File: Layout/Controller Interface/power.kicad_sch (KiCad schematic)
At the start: 26 parts, among them J6 Conn_01x02_Pin, Q1 AO3401A, Q2 AO3401A, Q3 AO3401A, Q4 AO3400A, Q5 AO3400A, SW5 SW_Push_Dual, U2 LM3671MF, U4 MCP73812T-420I-OT, U5 TPS613222ADBZ

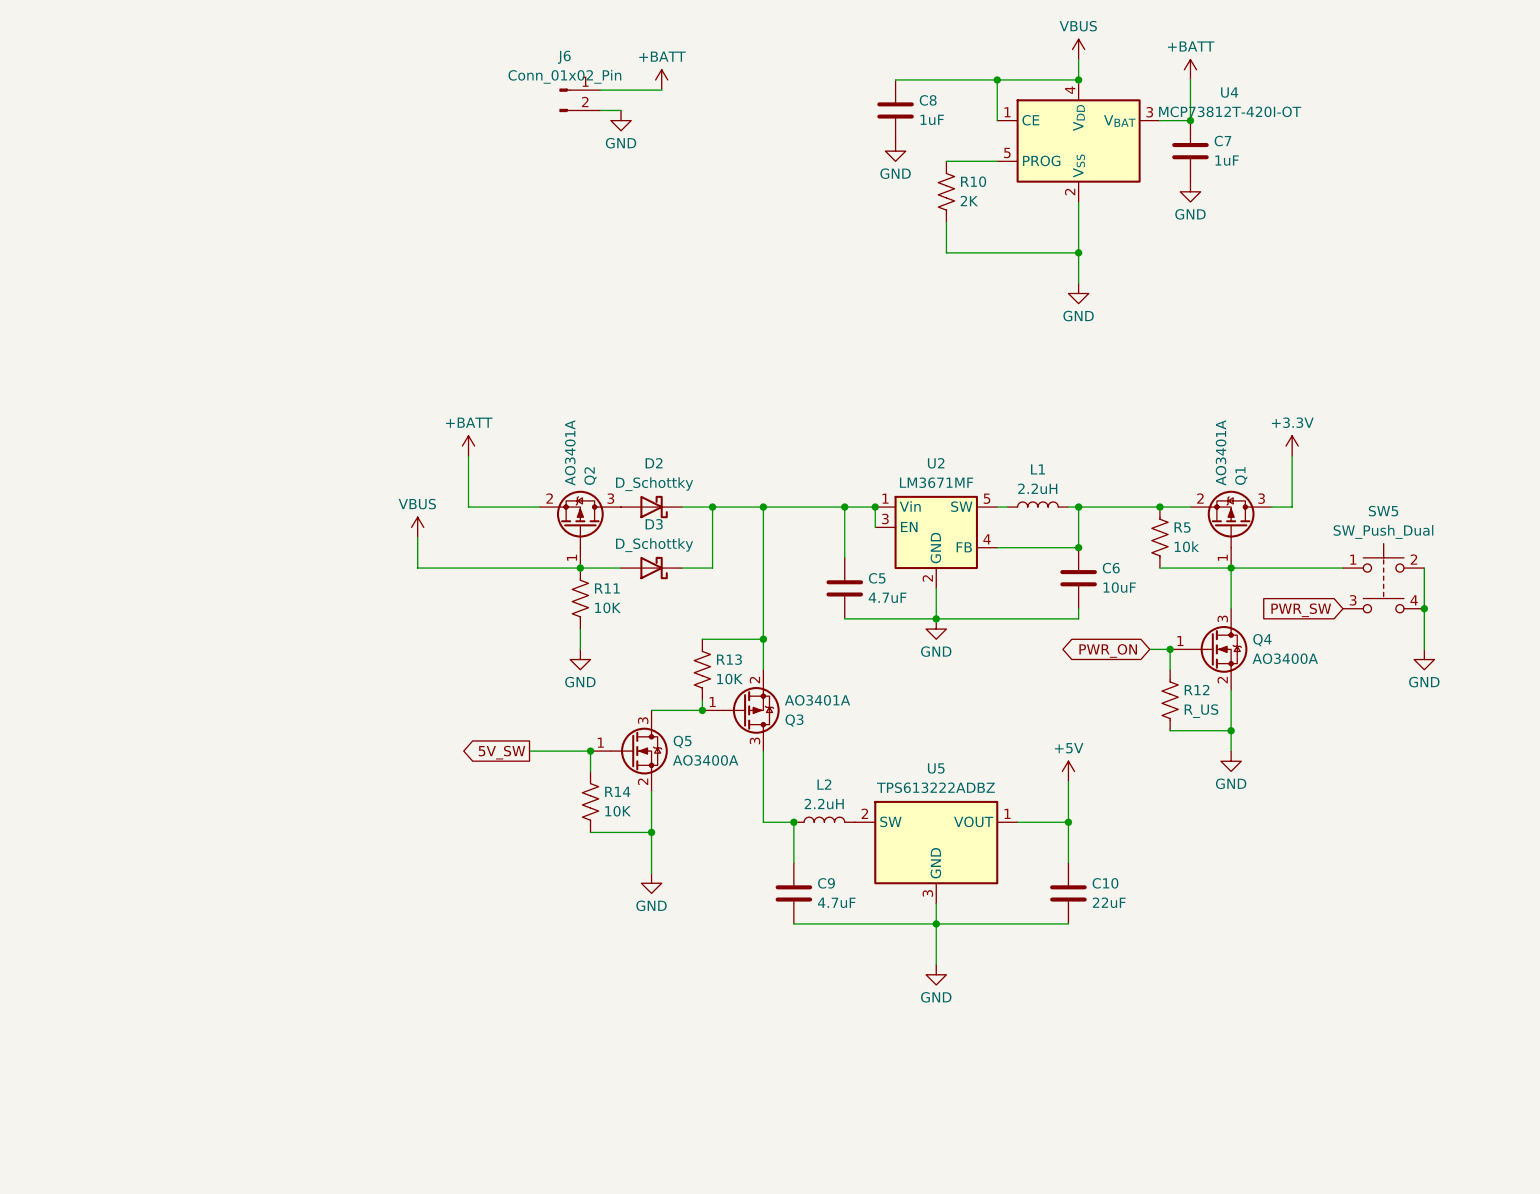
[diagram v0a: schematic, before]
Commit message: Schematic updates
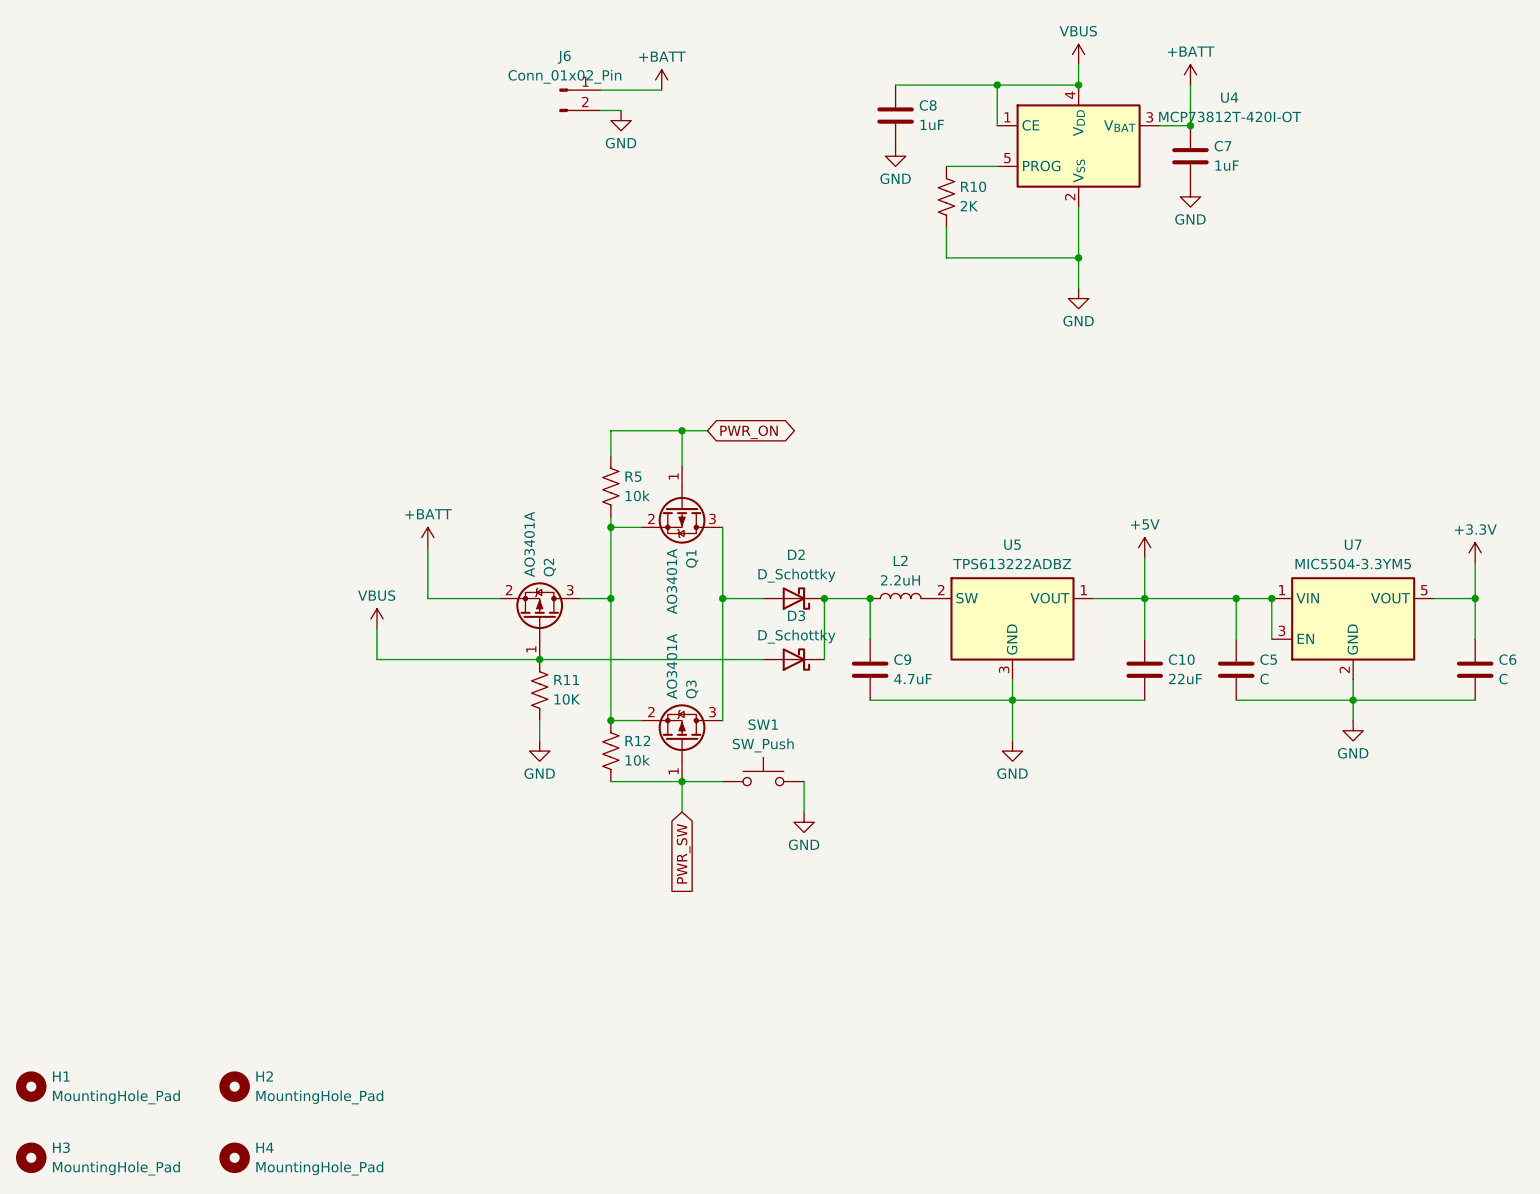
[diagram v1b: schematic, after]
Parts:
- removed L1: 2.2uH, symbol SparkFun-Coil:L
- removed Q4, Q5: AO3400A, Package_TO_SOT_SMD:SOT-23, symbol Transistor_FET:AO3400A
- removed R13, R14: 10K, symbol Device:R_US
- removed SW5: SW_Push_Dual, symbol Switch:SW_Push_Dual
- removed U2: LM3671MF, Package_TO_SOT_SMD:TSOT-23-5, symbol Regulator_Switching:LM3670MF
- added H1, H2, H3, H4: MountingHole_Pad, MountingHole:MountingHole_2.2mm_M2_DIN965, symbol Mechanical:MountingHole
- added SW1: SW_Push, Button_Switch_SMD:SW_SPST_TL3342, symbol Switch:SW_Push
- added U7: MIC5504-3.3YM5, Package_TO_SOT_SMD:SOT-23-5, symbol Regulator_Linear:MIC5504-3.3YM5
- C10, C7, C8, C9: footprint (none) -> Capacitor_SMD:C_0805_2012Metric
- C5: value 4.7uF -> C; footprint (none) -> Capacitor_SMD:C_0805_2012Metric
- C6: value 10uF -> C; footprint (none) -> Capacitor_SMD:C_0805_2012Metric
- D2, D3: footprint (none) -> Diode_SMD:D_0805_2012Metric
- J6: footprint (none) -> Connector_JST:JST_PH_S2B-PH-SM4-TB_1x02-1MP_P2.00mm_Horizontal
- L2: footprint (none) -> Inductor_SMD:L_0805_2012Metric
- R10, R11, R5: footprint (none) -> Resistor_SMD:R_0805_2012Metric
- R12: value R_US -> 10k; footprint (none) -> Resistor_SMD:R_0805_2012Metric
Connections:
- net +3.3V: now also C6.1, U7.5 (VOUT); no longer Q1.3 (D)
- net +5V: now also C5.1, U7.1 (VIN), U7.3 (EN)
- net GND: now also SW1.2, U7.2 (GND); no longer R12.2
- net PWR_ON: now also Q1.1 (G), R5.1; no longer R12.1
- net PWR_SW: now also Q3.1 (G), R12.2, SW1.1
- net at D2.1 (K), D3.1 (K): now also C9.1, L2.1; no longer C5.1, Q3.2 (S)
- net at Q1.2 (S), R5.2: now also Q2.3 (D), Q3.2 (S), R12.1; no longer C6.1
- net at D2.2 (A): now also Q1.3 (D), Q3.3 (D); no longer Q2.3 (D)
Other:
- moved on the sheet: C10, C7, C8, C9, D2, D3, L2, Q1, Q2, R10, R11, R5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

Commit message: Completed schematic and layout
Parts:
- removed H3, H4: MountingHole_Pad, MountingHole:MountingHole_2.2mm_M2_DIN965, symbol Mechanical:MountingHole
- SW1: value SW_Push -> PWR
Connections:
- net at Q1.2 (S), Q3.2 (S), R12.1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: no longer Q2.3 (D)
- net at D2.2 (A), Q1.3 (D), Q3.3 (D): now also Q2.3 (D)
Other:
- moved on the sheet: Q2, R11

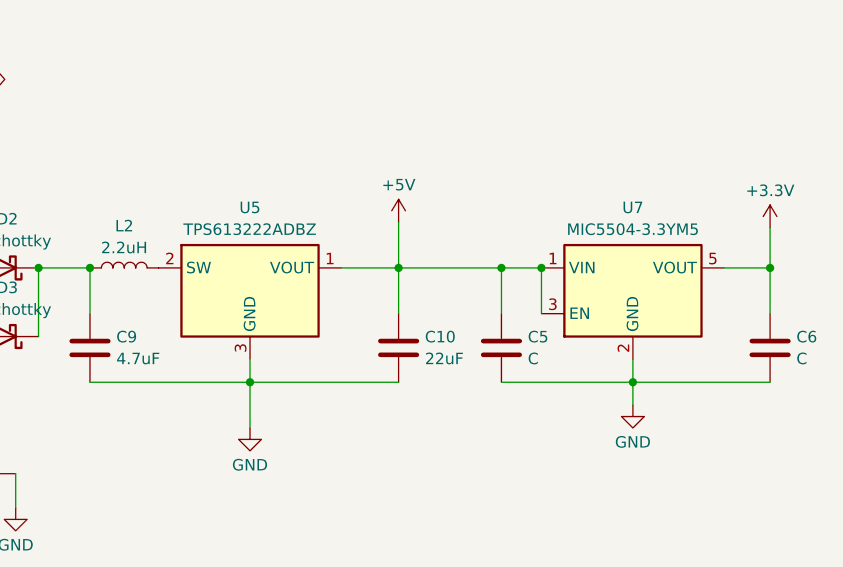
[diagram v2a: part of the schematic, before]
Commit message: Switching regulator footprint doesn't exist
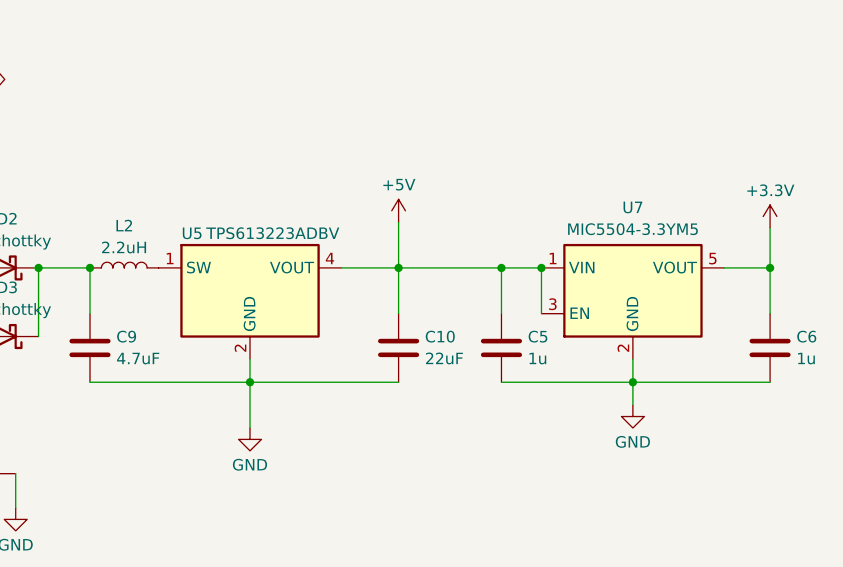
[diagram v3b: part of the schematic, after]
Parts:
- C5, C6: value C -> 1u
- U5: value TPS613222ADBZ -> TPS613223ADBV; footprint Package_TO_SOT_SMD:SOT-23 -> Package_TO_SOT_SMD:SOT-23-5; symbol Regulator_Switching:TPS613222ADBZ -> Regulator_Switching:TPS613223ADBV
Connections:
- net +5V: now also U5.4 (VOUT); no longer U5.1 (VOUT)
- net GND: now also U5.2 (GND); no longer U5.3 (GND)
- net at L2.2: now also U5.1 (SW); no longer U5.2 (SW)

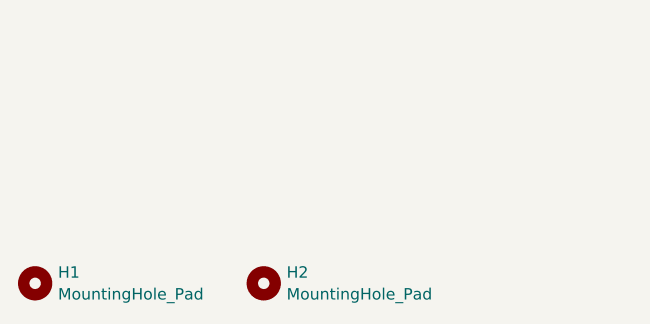
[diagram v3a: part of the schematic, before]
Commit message: Create a separate board for the LEDs
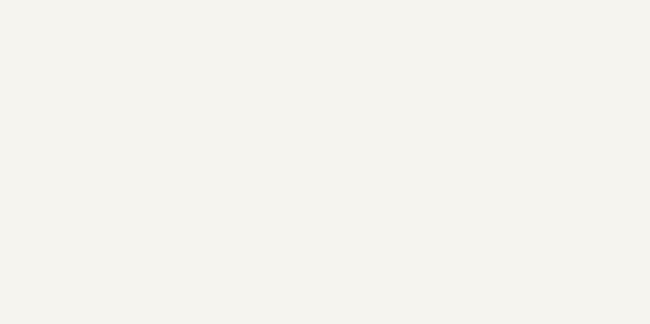
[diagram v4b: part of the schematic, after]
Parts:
- removed H1, H2: MountingHole_Pad, MountingHole:MountingHole_2.2mm_M2_DIN965, symbol Mechanical:MountingHole
- SW1: footprint Button_Switch_SMD:SW_SPST_TL3342 -> Button_Switch_SMD:Panasonic_EVQPUK_EVQPUB
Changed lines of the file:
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@@
-    )
-  )
-  (symbol (lib_id "Mechanical:MountingHole") (at 59.69 160.02 0) (unit 1)
-    (in_bom yes) (on_board yes) (dnp no) (fields_autoplaced)
-    (property "Reference" "H2" (at 62.23 158.8079 0)
-      (effects (font (size 1.27 1.27)) (justify left))
-    )
-    (property "Value" "MountingHole_Pad" (at 62.23 161.2321 0)
-      (effects (font (size 1.27 1.27)) (justify left))
-    )
-    (property "Footprint" "MountingHole:MountingHole_2.2mm_M2_DIN965" (at 59.69 160.02 0)
-      (effects (font (size 1.27 1.27)) hide)
-    )
-    (property "Datasheet" "~" (at 59.69 160.02 0)
-      (effects (font (size 1.27 1.27)) hide)
-    )
-    (instances
-      (project "Controller Interface"
-        (path "/debf4462-021e-4805-bcd2-6130c1f65c4c/0e5e425d-874a-4494-8f06-80e1d5ace878"
-          (reference "H2") (unit 1)
-        )
-      )
     )
   )
@@
     )
   )
-  (symbol (lib_id "Mechanical:MountingHole") (at 34.29 160.02 0) (unit 1)
-    (in_bom yes) (on_board yes) (dnp no) (fields_autoplaced)
-    (property "Reference" "H1" (at 36.83 158.8079 0)
-      (effects (font (size 1.27 1.27)) (justify left))
-    )
-    (property "Value" "MountingHole_Pad" (at 36.83 161.2321 0)
-      (effects (font (size 1.27 1.27)) (justify left))
-    )
-    (property "Footprint" "MountingHole:MountingHole_2.2mm_M2_DIN965" (at 34.29 160.02 0)
-      (effects (font (size 1.27 1.27)) hide)
-    )
-    (property "Datasheet" "~" (at 34.29 160.02 0)
-      (effects (font (size 1.27 1.27)) hide)
-    )
-    (instances
-      (project "Controller Interface"
-        (path "/debf4462-021e-4805-bcd2-6130c1f65c4c/0e5e425d-874a-4494-8f06-80e1d5ace878"
-          (reference "H1") (unit 1)
-        )
-      )
-    )
-  )
   (symbol (lib_id "power:GND") (at 81.28 116.84 0) (unit 1)
     (in_bom yes) (on_board yes) (dnp no) (fields_autoplaced)
@@
       (effects (font (size 1.27 1.27)))
     )
-    (property "Footprint" "Button_Switch_SMD:SW_SPST_TL3342" (at 125.73 116.84 0)
-      (effects (font (size 1.27 1.27)) hide)
-    )
+    (property "Footprint" "Button_Switch_SMD:Panasonic_EVQPUK_EVQPUB" (at 125.73 116.84 0)
+      (effects (font (size 1.27 1.27)) hide)
+    )

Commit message: Use separate board for lights
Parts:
- C10, C5, C6, C7, C8, C9: footprint Capacitor_SMD:C_0805_2012Metric -> Capacitor_SMD:C_0603_1608Metric
- R10, R11, R12, R5: footprint Resistor_SMD:R_0805_2012Metric -> Resistor_SMD:R_0603_1608Metric
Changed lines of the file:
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@@
       (effects (font (size 1.27 1.27)) (justify left))
     )
-    (property "Footprint" "Resistor_SMD:R_0805_2012Metric" (at 107.696 118.364 90)
+    (property "Footprint" "Resistor_SMD:R_0603_1608Metric" (at 107.696 118.364 90)
       (effects (font (size 1.27 1.27)) hide)
     )
@@
       (effects (font (size 1.27 1.27)) (justify left))
     )
-    (property "Footprint" "Resistor_SMD:R_0805_2012Metric" (at 107.696 85.344 90)
+    (property "Footprint" "Resistor_SMD:R_0603_1608Metric" (at 107.696 85.344 90)
       (effects (font (size 1.27 1.27)) hide)
     )
@@
       (effects (font (size 1.27 1.27)) (justify left))
     )
-    (property "Footprint" "Capacitor_SMD:C_0805_2012Metric" (at 140.0302 111.76 0)
+    (property "Footprint" "Capacitor_SMD:C_0603_1608Metric" (at 140.0302 111.76 0)
       (effects (font (size 1.27 1.27)) hide)
     )
@@
       (effects (font (size 1.27 1.27)) (justify right))
     )
-    (property "Footprint" "Resistor_SMD:R_0805_2012Metric" (at 80.264 110.236 90)
+    (property "Footprint" "Resistor_SMD:R_0603_1608Metric" (at 80.264 110.236 90)
       (effects (font (size 1.27 1.27)) hide)
     )
@@
       (effects (font (size 1.27 1.27)) (justify left))
     )
-    (property "Footprint" "Capacitor_SMD:C_0805_2012Metric" (at 143.2052 42.545 0)
+    (property "Footprint" "Capacitor_SMD:C_0603_1608Metric" (at 143.2052 42.545 0)
       (effects (font (size 1.27 1.27)) hide)
     )
@@
       (effects (font (size 1.27 1.27)) (justify left))
     )
-    (property "Footprint" "Capacitor_SMD:C_0805_2012Metric" (at 215.5952 111.76 0)
+    (property "Footprint" "Capacitor_SMD:C_0603_1608Metric" (at 215.5952 111.76 0)
       (effects (font (size 1.27 1.27)) hide)
     )
@@
       (effects (font (size 1.27 1.27)) (justify left))
     )
-    (property "Footprint" "Capacitor_SMD:C_0805_2012Metric" (at 185.7502 111.76 0)
+    (property "Footprint" "Capacitor_SMD:C_0603_1608Metric" (at 185.7502 111.76 0)
       (effects (font (size 1.27 1.27)) hide)
     )
@@
       (effects (font (size 1.27 1.27)) (justify left))
     )
-    (property "Footprint" "Capacitor_SMD:C_0805_2012Metric" (at 174.3202 111.76 0)
+    (property "Footprint" "Capacitor_SMD:C_0603_1608Metric" (at 174.3202 111.76 0)
       (effects (font (size 1.27 1.27)) hide)
     )
@@
       (effects (font (size 1.27 1.27)) (justify left))
     )
-    (property "Footprint" "Resistor_SMD:R_0805_2012Metric" (at 149.606 49.149 90)
+    (property "Footprint" "Resistor_SMD:R_0603_1608Metric" (at 149.606 49.149 90)
       (effects (font (size 1.27 1.27)) hide)
     )
@@
       (effects (font (size 1.27 1.27)) (justify left))
     )
-    (property "Footprint" "Capacitor_SMD:C_0805_2012Metric" (at 180.0352 47.625 0)
-      (effects (font (size 1.27 1.27)) hide)
-    )
+    (property "Footprint" "Capacitor_SMD:C_0603_1608Metric" (at 180.0352 47.625 0)
+      (effects (font (size 1.27 1.27)) hide)
+    )
